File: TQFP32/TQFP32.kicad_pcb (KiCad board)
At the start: 2 copper layers, 40.6 x 17.8 mm, 8 parts, among them J1 Conn_01x16, J2 Conn_01x16, J3 Conn_02x16_Counter_Clockwise, J4 Conn_02x16_Counter_Clockwise

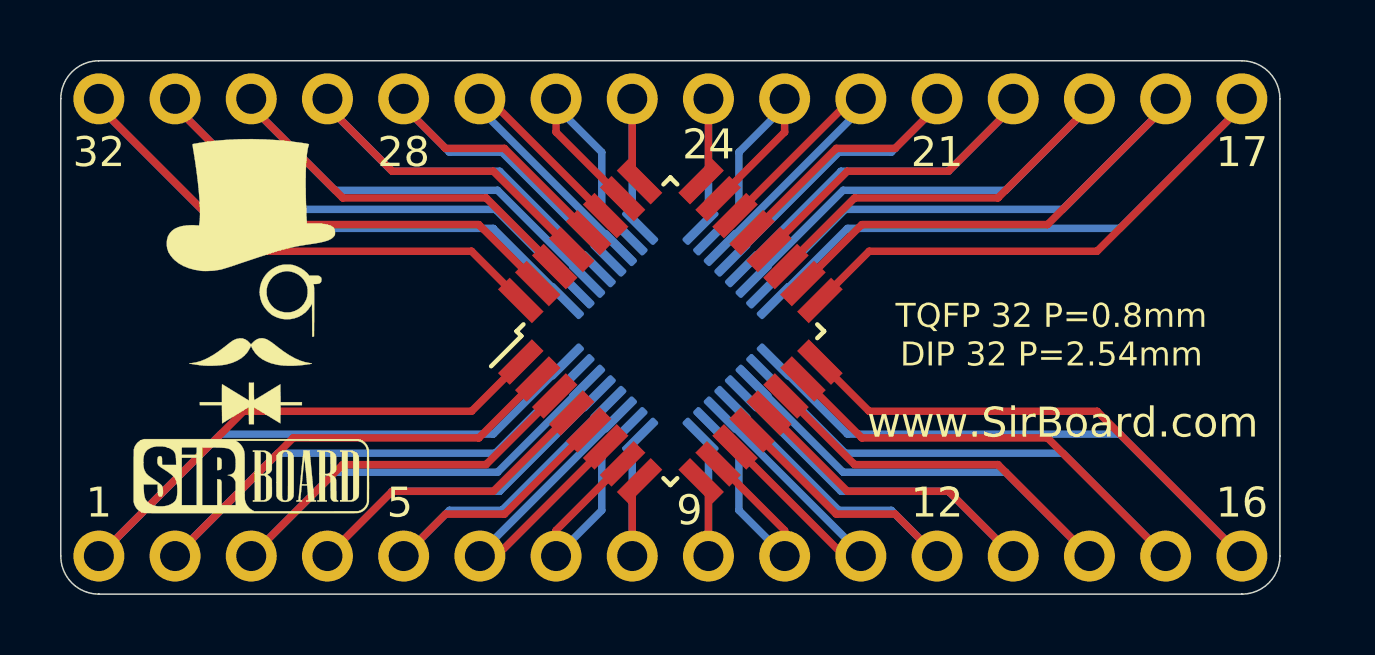
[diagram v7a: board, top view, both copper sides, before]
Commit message: Breakout Boards Revision 2
Renders updated, silkscreen text improved, blurry silkscreen items removed/resized.
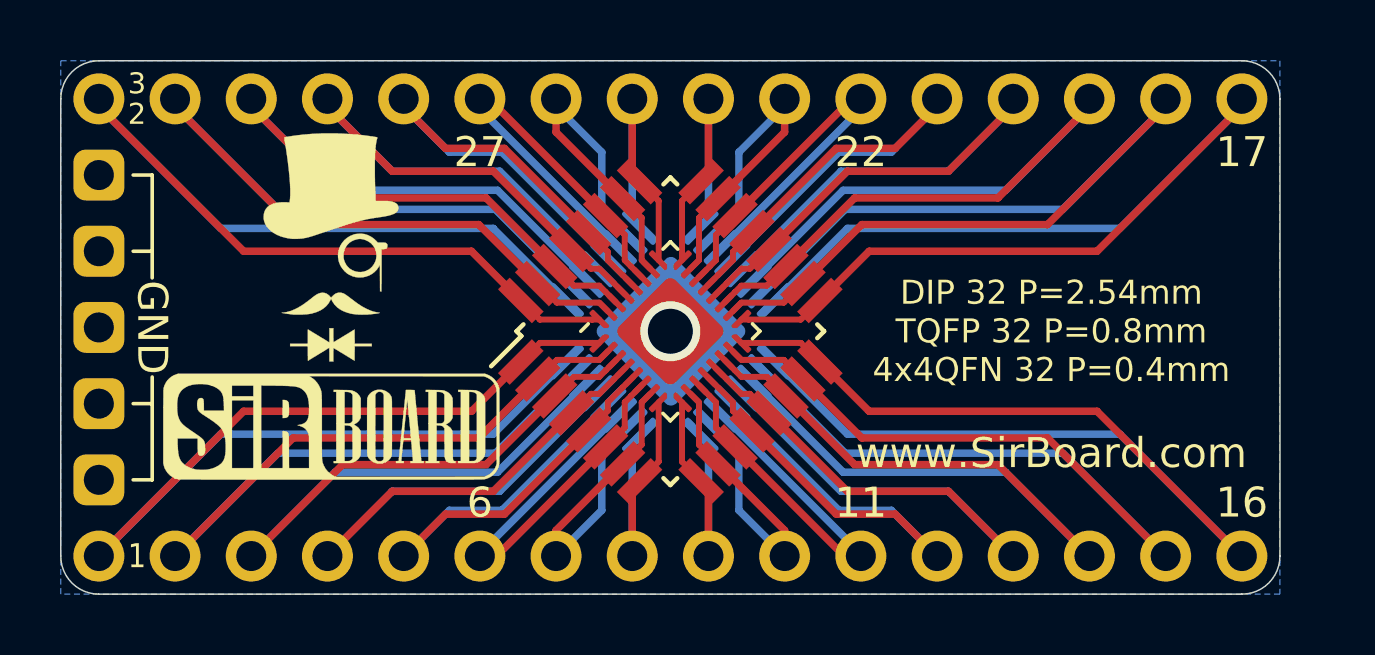
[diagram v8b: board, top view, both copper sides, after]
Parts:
- removed the G*** at (79.9, 39.4)
- removed the G*** at (79.9, 32.9)
- added ?: , , B.Cu at (66.0, 34.6)
- added G***: LOGO, logo:SirBoard112x35, B.Cu at (78.6, 38.1)
- added G***: LOGO, logo:logo76x107, B.Cu at (78.6, 32.3)
- added J5: Conn_02x16_Counter_Clockwise, Package_DFN_QFN:QFN-32-1EP_4x4mm_P0.4mm_EP2.65x2.65mm, F.Cu at (65.9, 34.7)
- added J6: Conn_01x05, Connector_PinHeader_2.54mm:PinHeader_1x05_P2.54mm_Vertical, F.Cu at (46.9, 29.5)
- G***: footprint logo:logo94x134 -> logo:logo76x107
- G***: footprint logo:SirBoard79x25 -> logo:SirBoard112x35
- moved G*** 3.14 mm to (54.6, 37.8)
- moved G*** 2.90 mm to (54.6, 31.9)
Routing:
- net Net-(J1-Pad9): track 6.73 -> 9.61 mm
- net Net-(J1-Pad8): track 6.73 -> 9.61 mm
- net Net-(J2-Pad8): track 6.73 -> 9.61 mm
- net Net-(J2-Pad9): track 6.73 -> 9.61 mm
- net Net-(J1-Pad16): track 35.0 -> 37.9 mm
- net Net-(J2-Pad16): track 35.0 -> 37.9 mm
- net Net-(J1-Pad1): track 35.0 -> 37.9 mm
- net Net-(J2-Pad1): track 35.0 -> 37.9 mm
- net Net-(J2-Pad15): track 30.5 -> 33.2 mm
- net Net-(J2-Pad2): track 30.5 -> 33.2 mm
- net Net-(J1-Pad15): track 30.5 -> 33.2 mm
- net Net-(J1-Pad10): track 9.37 -> 12.1 mm
- net Net-(J2-Pad10): track 9.37 -> 12.1 mm
- net Net-(J1-Pad2): track 30.5 -> 33.2 mm
- net Net-(J1-Pad7): track 9.37 -> 12.1 mm
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- added copper zone on B.Cu, net GND
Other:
- net class Default: clearance 0.2 -> 0.127; trace_width 0.25 -> 0.127; via_dia 0.8 -> 0.6; via_drill 0.4 -> 0.3
- rule trace_clearance: 0.2 -> 0.127
- rule trace_min: 0.2 -> 0.127
- board text added: "11"
- board text added: "2"
- board text added: "20"
- board text added: "22"
- board text added: "27"
- board text added: "3"
- board text added: "6"
- board text added: "7"
- board text added: "DIP 32 P=2.54mm TQFP 32 P=0.8mm 4x4QFN 32 P=0.4mm"
- board text added: "GND"
- board text removed: "12"
- board text removed: "21"
- board text removed: "24"
- board text removed: "28"
- board text removed: "5"
- board text removed: "9"
- board text removed: "TQFP 32 P=0.8mm DIP 32 P=2.54mm"
